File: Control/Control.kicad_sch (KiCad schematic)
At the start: 9 parts, among them J1 Conn_01x04_Pin, J2 Conn_01x08_Pin, J3 Conn_01x08_Pin, J4 Conn_01x07_Pin, U1 AT28C64B-15PI, U2 AT28C64B-15PI, U3 SN74AC14N, U4 SN74AC14N

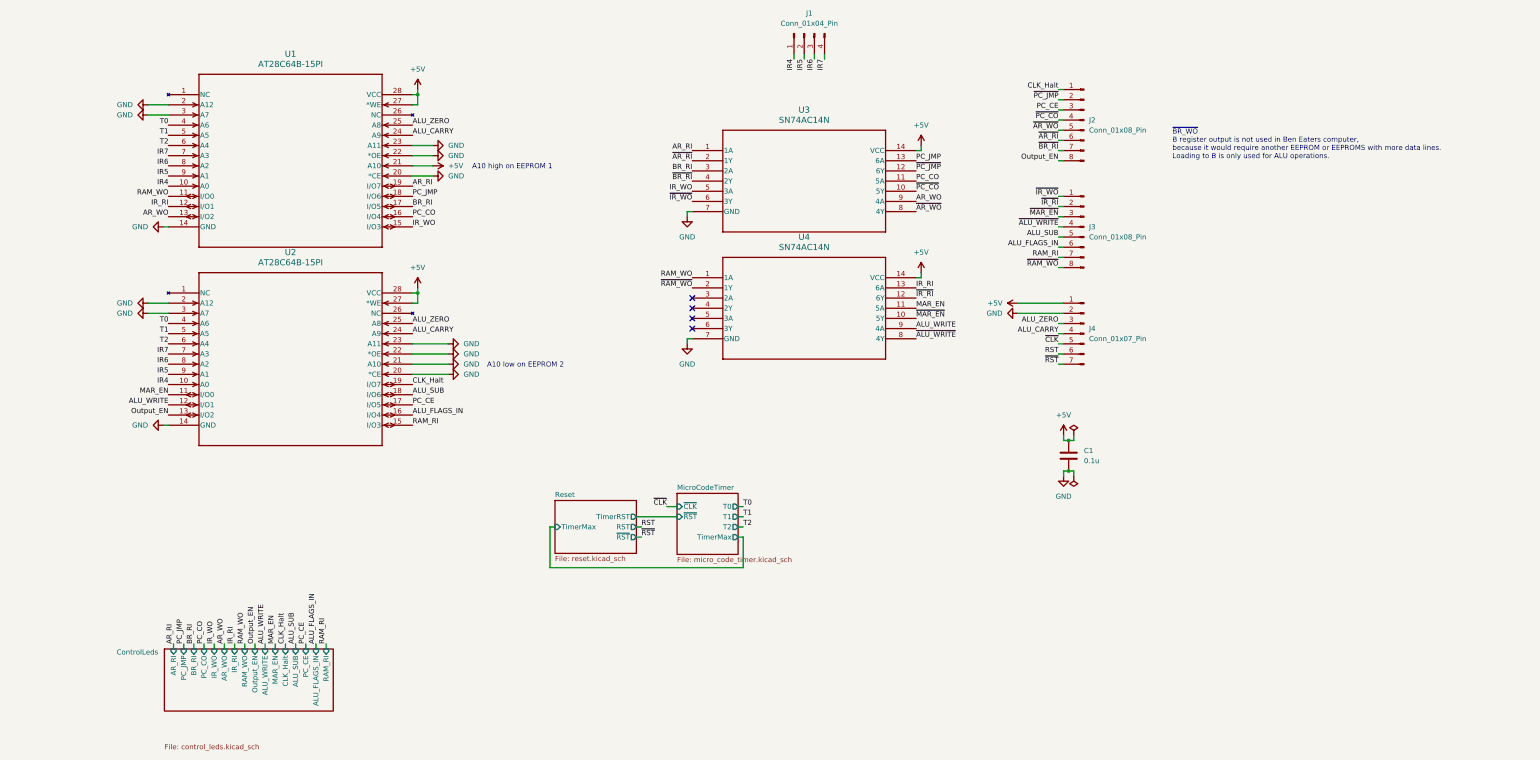
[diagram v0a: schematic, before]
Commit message: Control routed on PCB
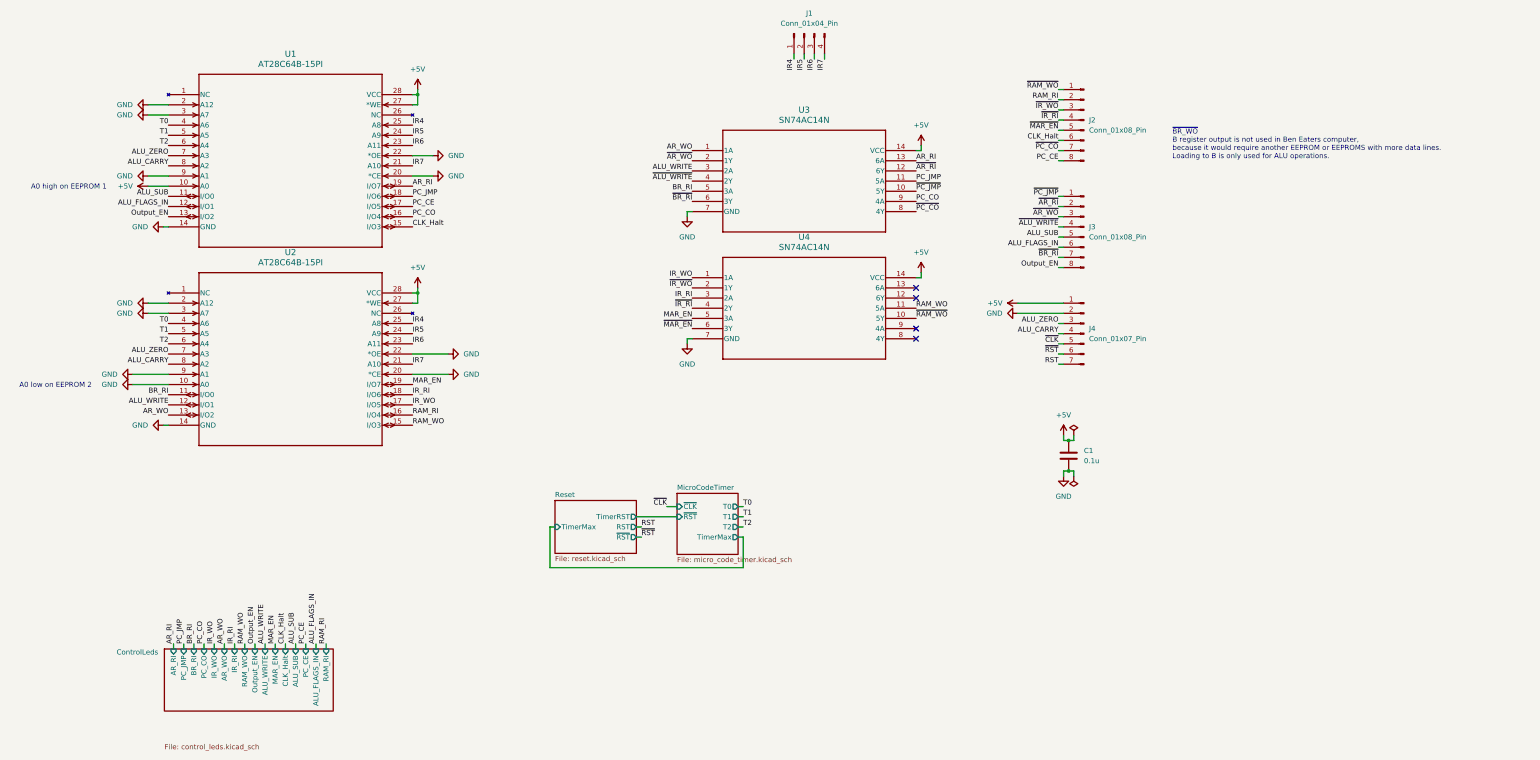
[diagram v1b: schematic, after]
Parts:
- C1: footprint (none) -> Capacitor_THT:C_Disc_D5.0mm_W2.5mm_P2.50mm
- J1: footprint (none) -> Connector_PinHeader_2.54mm:PinHeader_1x04_P2.54mm_Vertical
- J2, J3: footprint (none) -> Connector_PinHeader_2.54mm:PinHeader_1x08_P2.54mm_Vertical
- J4: footprint (none) -> Connector_PinHeader_2.54mm:PinHeader_1x07_P2.54mm_Vertical
- U1, U2: footprint 28P6 -> _DownloadFootprints:eeprom
- U3, U4: footprint N14 -> _DownloadFootprints:6x_not
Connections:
- net +5V: now also U1.10 (A0); no longer U1.21 (A10)
- net ALU_CARRY: now also U1.8 (A2), U2.8 (A2); no longer U1.24 (A9), U2.24 (A9)
- net ALU_FLAGS_IN: now also U1.12 (I/O1); no longer U2.16 (I/O4)
- net ALU_SUB: now also U1.11 (I/O0); no longer U2.18 (I/O6)
- net ALU_WRITE: now also U3.3 (2A); no longer U4.9 (4A)
- net ALU_ZERO: now also U1.7 (A3), U2.7 (A3); no longer U1.25 (A8), U2.25 (A8)
- net AR_RI: now also U3.13 (6A); no longer U3.1 (1A)
- net AR_WO: now also U2.13 (I/O2), U3.1 (1A); no longer U1.13 (I/O2), U3.9 (4A)
- net BR_RI: now also U2.11 (I/O0), U3.5 (3A); no longer U1.17 (I/O5), U3.3 (2A)
- net CLK_Halt: now also J2.6 (Pin_6), U1.15 (I/O3); no longer J2.1 (Pin_1), U2.19 (I/O7)
- net GND: now also U1.9 (A1), U2.10 (A0), U2.9 (A1); no longer U1.23 (A11), U2.21 (A10), U2.23 (A11)
- net IR4: now also U1.25 (A8), U2.25 (A8); no longer U1.10 (A0), U2.10 (A0)
- net IR5: now also U1.24 (A9), U2.24 (A9); no longer U1.9 (A1), U2.9 (A1)
- net IR6: now also U1.23 (A11), U2.23 (A11); no longer U1.8 (A2), U2.8 (A2)
- net IR7: now also U1.21 (A10), U2.21 (A10); no longer U1.7 (A3), U2.7 (A3)
- net IR_RI: now also U2.18 (I/O6), U4.3 (2A); no longer U1.12 (I/O1), U4.13 (6A)
- net IR_WO: now also U2.17 (I/O5), U4.1 (1A); no longer U1.15 (I/O3), U3.5 (3A)
- net MAR_EN: now also U2.19 (I/O7), U4.5 (3A); no longer U2.11 (I/O0), U4.11 (5A)
- net Output_EN: now also J3.8 (Pin_8), U1.13 (I/O2); no longer J2.8 (Pin_8), U2.13 (I/O2)
- net PC_CE: now also J2.8 (Pin_8), U1.17 (I/O5); no longer J2.3 (Pin_3), U2.17 (I/O5)
- net PC_CO: now also U3.9 (4A); no longer U3.11 (5A)
- net PC_JMP: now also U3.11 (5A); no longer U3.13 (6A)
- net RAM_RI: now also J2.2 (Pin_2), U2.16 (I/O4); no longer J3.7 (Pin_7), U2.15 (I/O3)
- net RAM_WO: now also U2.15 (I/O3), U4.11 (5A); no longer U1.11 (I/O0), U4.1 (1A)
- net RST: now also J4.7 (Pin_7); no longer J4.6 (Pin_6)
- net ~{ALU_WRITE}: now also U3.4 (2Y); no longer U4.8 (4Y)
- net ~{AR_RI}: now also J3.2 (Pin_2), U3.12 (6Y); no longer J2.6 (Pin_6), U3.2 (1Y)
- net ~{AR_WO}: now also J3.3 (Pin_3), U3.2 (1Y); no longer J2.5 (Pin_5), U3.8 (4Y)
- net ~{BR_RI}: now also J3.7 (Pin_7), U3.6 (3Y); no longer J2.7 (Pin_7), U3.4 (2Y)
- net ~{IR_RI}: now also J2.4 (Pin_4), U4.4 (2Y); no longer J3.2 (Pin_2), U4.12 (6Y)
- net ~{IR_WO}: now also J2.3 (Pin_3), U4.2 (1Y); no longer J3.1 (Pin_1), U3.6 (3Y)
- net ~{MAR_EN}: now also J2.5 (Pin_5), U4.6 (3Y); no longer J3.3 (Pin_3), U4.10 (5Y)
- net ~{PC_CO}: now also J2.7 (Pin_7), U3.8 (4Y); no longer J2.4 (Pin_4), U3.10 (5Y)
- net ~{PC_JMP}: now also J3.1 (Pin_1), U3.10 (5Y); no longer J2.2 (Pin_2), U3.12 (6Y)
- net ~{RAM_WO}: now also J2.1 (Pin_1), U4.10 (5Y); no longer J3.8 (Pin_8), U4.2 (1Y)
- net ~{RST}: now also J4.6 (Pin_6); no longer J4.7 (Pin_7)
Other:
- note added: "A0 high on EEPROM 1"
- note added: "A0 low on EEPROM 2"
- note removed: "A10 high on EEPROM 1"
- note removed: "A10 low on EEPROM 2"

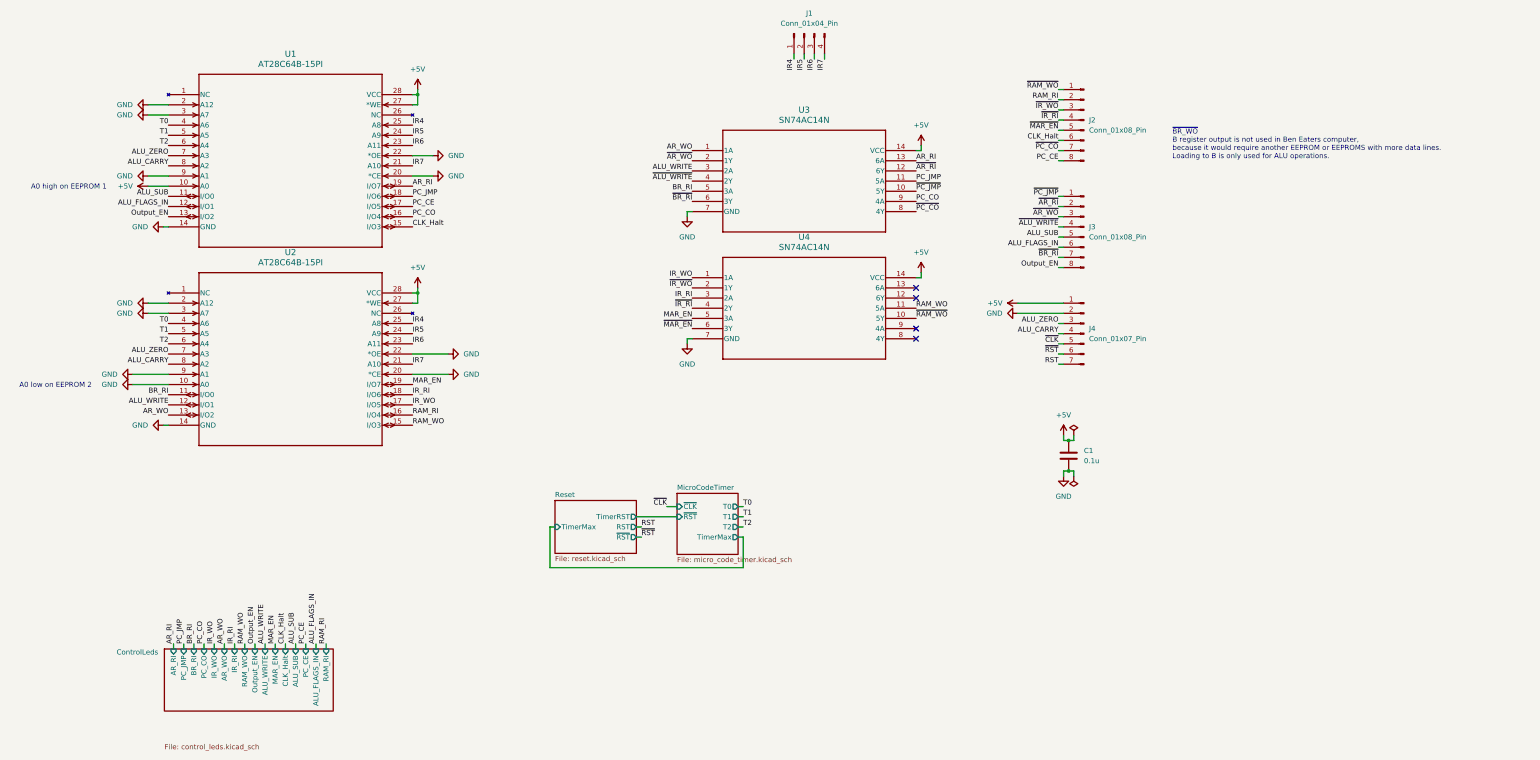
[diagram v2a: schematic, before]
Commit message: Added spare pins to control
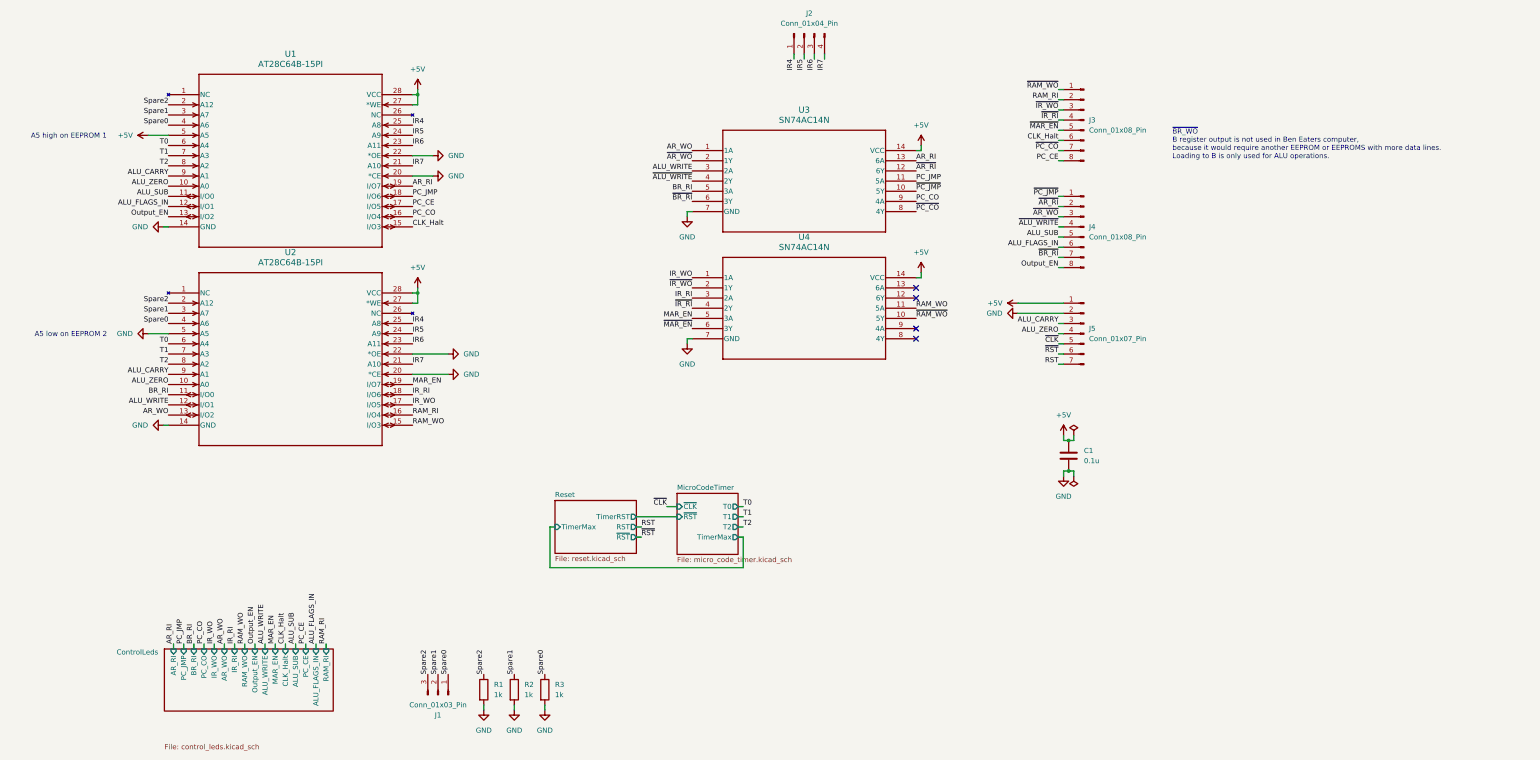
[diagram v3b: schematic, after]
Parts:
- added J1: Conn_01x03_Pin, Connector_PinHeader_2.54mm:PinHeader_1x03_P2.54mm_Vertical, symbol Connector:Conn_01x03_Pin
- added R1, R2, R3: 1k, _DownloadFootprints:CF_series_Resistors_THT, symbol Device:R
- renumbered J1 to J2, J2 to J3, J3 to J4, J4 to J5
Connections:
- net +5V: now also U1.5 (A5); no longer U1.10 (A0)
- net ALU_CARRY: now also J5.3 (Pin_3), U1.9 (A1), U2.9 (A1); no longer J5.4 (Pin_4), U1.8 (A2), U2.8 (A2)
- net ALU_ZERO: now also J5.4 (Pin_4), U1.10 (A0), U2.10 (A0); no longer J5.3 (Pin_3), U1.7 (A3), U2.7 (A3)
- net GND: now also U2.5 (A5), R1.2, R2.2, R3.2; no longer U1.2 (A12), U1.3 (A7), U1.9 (A1), U2.10 (A0), U2.2 (A12), U2.3 (A7), U2.9 (A1)
- net T0: now also U1.6 (A4), U2.6 (A4); no longer U1.4 (A6), U2.4 (A6)
- net T1: now also U1.7 (A3), U2.7 (A3); no longer U1.5 (A5), U2.5 (A5)
- net T2: now also U1.8 (A2), U2.8 (A2); no longer U1.6 (A4), U2.6 (A4)
- new net Spare0: J1.1 (Pin_1), R3.1, U1.4 (A6), U2.4 (A6)
- new net Spare1: J1.2 (Pin_2), R2.1, U1.3 (A7), U2.3 (A7)
- new net Spare2: J1.3 (Pin_3), R1.1, U1.2 (A12), U2.2 (A12)
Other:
- note added: "A5 high on EEPROM 1"
- note added: "A5 low on EEPROM 2"
- note removed: "A0 high on EEPROM 1"
- note removed: "A0 low on EEPROM 2"

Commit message: Output enable should be active low so I updated control to pass it through an inverter
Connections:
- net ALU_FLAGS_IN: now also U1.13 (I/O2); no longer U1.12 (I/O1)
- net ALU_SUB: now also U1.12 (I/O1); no longer U1.11 (I/O0)
- net ALU_WRITE: now also U2.13 (I/O2), U3.1 (1A); no longer U2.12 (I/O1), U3.3 (2A)
- net AR_RI: now also U3.11 (5A); no longer U3.13 (6A)
- net AR_WO: now also U1.18 (I/O6), U3.13 (6A); no longer U2.13 (I/O2), U3.1 (1A)
- net BR_RI: now also U2.12 (I/O1), U3.3 (2A); no longer U2.11 (I/O0), U3.5 (3A)
- net CLK_Halt: now also U1.16 (I/O4); no longer U1.15 (I/O3)
- net IR_RI: now also U4.1 (1A); no longer U4.3 (2A)
- net IR_WO: now also U2.16 (I/O4), U4.11 (5A); no longer U2.17 (I/O5), U4.1 (1A)
- net MAR_EN: now also U4.3 (2A); no longer U4.5 (3A)
- net Output_EN: now also U2.11 (I/O0), U3.5 (3A); no longer J4.8 (Pin_8), U1.13 (I/O2)
- net PC_CO: now also U1.15 (I/O3), U4.5 (3A); no longer U1.16 (I/O4), U3.9 (4A)
- net PC_JMP: now also U1.11 (I/O0), U3.9 (4A); no longer U1.18 (I/O6), U3.11 (5A)
- net RAM_RI: now also U2.17 (I/O5); no longer U2.16 (I/O4)
- net RAM_WO: now also U4.13 (6A); no longer U4.11 (5A)
- net ~{ALU_WRITE}: now also U3.2 (1Y); no longer U3.4 (2Y)
- net ~{AR_RI}: now also U3.10 (5Y); no longer U3.12 (6Y)
- net ~{AR_WO}: now also U3.12 (6Y); no longer U3.2 (1Y)
- net ~{BR_RI}: now also U3.4 (2Y); no longer U3.6 (3Y)
- net ~{IR_RI}: now also U4.2 (1Y); no longer U4.4 (2Y)
- net ~{IR_WO}: now also U4.10 (5Y); no longer U4.2 (1Y)
- net ~{MAR_EN}: now also U4.4 (2Y); no longer U4.6 (3Y)
- net ~{PC_CO}: now also U4.6 (3Y); no longer U3.8 (4Y)
- net ~{PC_JMP}: now also U3.8 (4Y); no longer U3.10 (5Y)
- net ~{RAM_WO}: now also U4.12 (6Y); no longer U4.10 (5Y)
- new net Output_~{EN}: J4.8 (Pin_8), U3.6 (3Y)
- no-connect marks 4 -> 2
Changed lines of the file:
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@@
-	)
-	(no_connect
-		(at 226.06 81.28)
-	)
-	(no_connect
-		(at 226.06 83.82)
 	)
 	(no_connect
@@
 	)
 	(label "ALU_SUB"
-		(at 39.37 58.42 180)
+		(at 39.37 60.96 180)
 		(fields_autoplaced yes)
 		(effects
@@
 	)
 	(label "MAR_EN"
-		(at 170.18 88.9 180)
+		(at 170.18 83.82 180)
 		(fields_autoplaced yes)
 		(effects
@@
 	)
 	(label "~{RAM_WO}"
-		(at 226.06 88.9 0)
+		(at 226.06 83.82 0)
 		(fields_autoplaced yes)
 		(effects
@@
 	)
 	(label "PC_JMP"
-		(at 226.06 54.61 0)
+		(at 226.06 59.69 0)
 		(fields_autoplaced yes)
 		(effects
@@
 	)
 	(label "~{ALU_WRITE}"
-		(at 170.18 54.61 180)
+		(at 170.18 49.53 180)
 		(fields_autoplaced yes)
 		(effects
@@
 	)
 	(label "ALU_WRITE"
-		(at 39.37 110.49 180)
+		(at 39.37 113.03 180)
 		(fields_autoplaced yes)
 		(effects
@@
 	)
 	(label "ALU_FLAGS_IN"
-		(at 39.37 60.96 180)
+		(at 39.37 63.5 180)
 		(fields_autoplaced yes)
 		(effects
@@
 	)
 	(label "IR_WO"
-		(at 170.18 78.74 180)
-		(fields_autoplaced yes)
-		(effects
-			(font
-				(size 1.27 1.27)
-			)
-			(justify right bottom)
+		(at 226.06 86.36 0)
+		(fields_autoplaced yes)
+		(effects
+			(font
+				(size 1.27 1.27)
+			)
+			(justify left bottom)
 		)
 	)
 	(label "IR_WO"
-		(at 100.33 110.49 0)
+		(at 100.33 113.03 0)
 		(fields_autoplaced yes)
 		(effects
@@
 	)
 	(label "~{BR_RI}"
-		(at 170.18 59.69 180)
+		(at 170.18 54.61 180)
+		(fields_autoplaced yes)
+		(effects
+			(font
+				(size 1.27 1.27)
+			)
+			(justify right bottom)
+		)
+	)
+	(label "Output_EN"
+		(at 170.18 57.15 180)
 		(fields_autoplaced yes)
 		(effects
@@
 	)
 	(label "ALU_WRITE"
-		(at 170.18 52.07 180)
+		(at 170.18 46.99 180)
 		(fields_autoplaced yes)
 		(effects
@@
 	)
 	(label "PC_CO"
-		(at 226.06 59.69 0)
-		(fields_autoplaced yes)
-		(effects
-			(font
-				(size 1.27 1.27)
-			)
-			(justify left bottom)
+		(at 170.18 88.9 180)
+		(fields_autoplaced yes)
+		(effects
+			(font
+				(size 1.27 1.27)
+			)
+			(justify right bottom)
 		)
 	)
@@
 		)
 	)
+	(label "Output_~{EN}"
+		(at 170.18 59.69 180)
+		(fields_autoplaced yes)
+		(effects
+			(font
+				(size 1.27 1.27)
+			)
+			(justify right bottom)
+		)
+	)
 	(label "RAM_RI"
 		(at 261.62 34.29 180)
@@
 	)
 	(label "BR_RI"
-		(at 39.37 107.95 180)
+		(at 39.37 110.49 180)
 		(fields_autoplaced yes)
 		(effects
@@
 	)
 	(label "AR_WO"
-		(at 39.37 113.03 180)
-		(fields_autoplaced yes)
-		(effects
-			(font
-				(size 1.27 1.27)
-			)
-			(justify right bottom)
+		(at 100.33 58.42 0)
+		(fields_autoplaced yes)
+		(effects
+			(font
+				(size 1.27 1.27)
+			)
+			(justify left bottom)
 		)
 	)
@@
 	)
 	(label "~{IR_RI}"
-		(at 170.18 86.36 180)
+		(at 170.18 81.28 180)
 		(fields_autoplaced yes)
 		(effects
@@
 	)
 	(label "~{MAR_EN}"
-		(at 170.18 91.44 180)
+		(at 170.18 86.36 180)
 		(fields_autoplaced yes)
 		(effects
@@
 	)
 	(label "~{PC_CO}"
-		(at 226.06 62.23 0)
-		(fields_autoplaced yes)
-		(effects
-			(font
-				(size 1.27 1.27)
-			)
-			(justify left bottom)
+		(at 170.18 91.44 180)
+		(fields_autoplaced yes)
+		(effects
+			(font
+				(size 1.27 1.27)
+			)
+			(justify right bottom)
 		)
 	)
 	(label "Output_EN"
-		(at 39.37 63.5 180)
+		(at 39.37 107.95 180)
 		(fields_autoplaced yes)
 		(effects
@@
 	)
 	(label "RAM_RI"
-		(at 100.33 113.03 0)
+		(at 100.33 110.49 0)
 		(fields_autoplaced yes)
 		(effects
@@
 	)
 	(label "AR_WO"
-		(at 170.18 46.99 180)
-		(fields_autoplaced yes)
-		(effects
-			(font
-				(size 1.27 1.27)
-			)
-			(justify right bottom)
+		(at 226.06 49.53 0)
+		(fields_autoplaced yes)
+		(effects
+			(font
+				(size 1.27 1.27)
+			)
+			(justify left bottom)
 		)
 	)
@@
 	)
 	(label "RAM_WO"
-		(at 226.06 86.36 0)
+		(at 226.06 81.28 0)
 		(fields_autoplaced yes)
 		(effects
@@
 	)
 	(label "~{AR_RI}"
+		(at 226.06 57.15 0)
+		(fields_autoplaced yes)
+		(effects
+			(font
+				(size 1.27 1.27)
+			)
+			(justify left bottom)
+		)
+	)
+	(label "~{AR_WO}"
 		(at 226.06 52.07 0)
 		(fields_autoplaced yes)
@@
 			)
 			(justify left bottom)
-		)
-	)
-	(label "~{AR_WO}"
-		(at 170.18 49.53 180)
-		(fields_autoplaced yes)
-		(effects
-			(font
-				(size 1.27 1.27)
-			)
-			(justify right bottom)
 		)
 	)
@@
 	)
 	(label "CLK_Halt"
-		(at 100.33 66.04 0)
+		(at 100.33 63.5 0)
 		(fields_autoplaced yes)
 		(effects
@@
 	)
 	(label "BR_RI"
-		(at 170.18 57.15 180)
+		(at 170.18 52.07 180)
 		(fields_autoplaced yes)
 		(effects
@@
 	)
 	(label "~{PC_JMP}"
-		(at 226.06 57.15 0)
+		(at 226.06 62.23 0)
 		(fields_autoplaced yes)
 		(effects
@@
 	)
 	(label "PC_JMP"
-		(at 100.33 58.42 0)
-		(fields_autoplaced yes)
-		(effects
-			(font
-				(size 1.27 1.27)
-			)
-			(justify left bottom)
+		(at 39.37 58.42 180)
+		(fields_autoplaced yes)
+		(effects
+			(font
+				(size 1.27 1.27)
+			)
+			(justify right bottom)
 		)
 	)
@@
 		)
 	)
-	(label "Output_EN"
+	(label "Output_~{EN}"
 		(at 261.62 76.2 180)
 		(fields_autoplaced yes)
@@
 	)
 	(label "AR_RI"
-		(at 226.06 49.53 0)
+		(at 226.06 54.61 0)
 		(fields_autoplaced yes)
 		(effects
@@
 	)
 	(label "IR_RI"
-		(at 170.18 83.82 180)
+		(at 170.18 78.74 180)
 		(fields_autoplaced yes)
 		(effects
@@
 	)
 	(label "~{IR_WO}"
-		(at 170.18 81.28 180)
-		(fields_autoplaced yes)
-		(effects
-			(font
-				(size 1.27 1.27)
-			)
-			(justify right bottom)
+		(at 226.06 88.9 0)
+		(fields_autoplaced yes)
+		(effects
+			(font
+				(size 1.27 1.27)
+			)
+			(justify left bottom)
 		)
 	)
@@
 	)
 	(label "PC_CO"
-		(at 100.33 63.5 0)
-		(fields_autoplaced yes)
-		(effects
+		(at 100.33 66.04 0)
+		(fields_autoplaced yes)
+		(effects
